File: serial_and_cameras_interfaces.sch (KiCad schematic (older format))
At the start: 60 parts, among them J13 533980471, J15 533980471, J16 533980471, J17 533980471, J2 WE_68715014522, U16 NTS0102GT, U17 NTS0104PW,118, U18 MAX485EESA, U5 NTS0102GT, U6 PCA9547BS

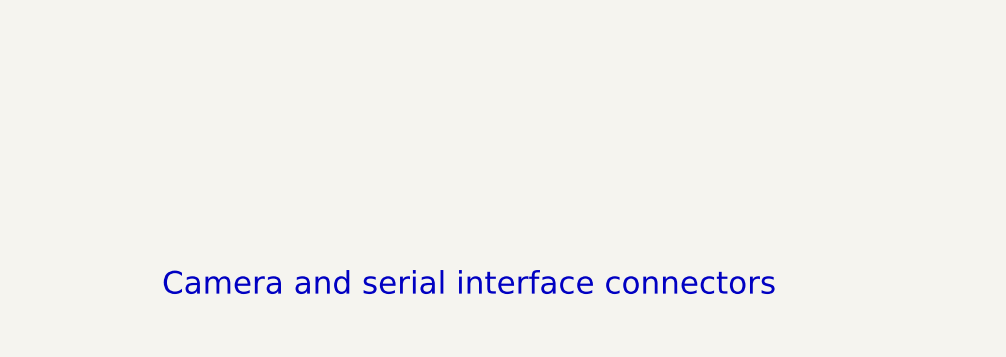
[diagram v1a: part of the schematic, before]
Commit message: Update the sch signage, remove redundant sheets
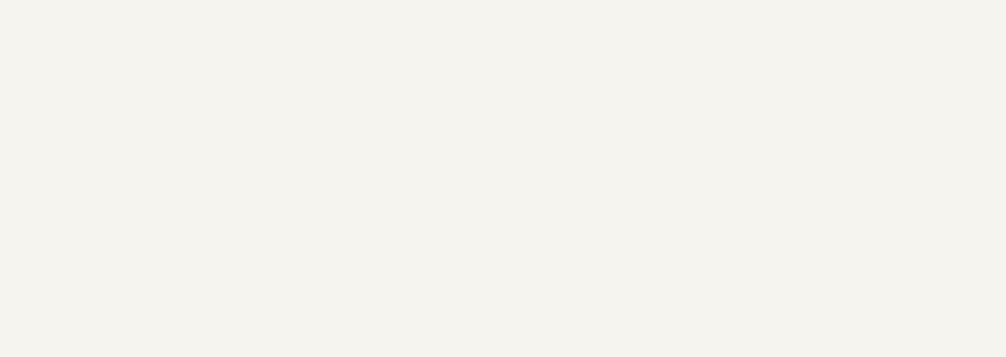
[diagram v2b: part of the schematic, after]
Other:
- note removed: "Camera and serial interface connectors\n"
